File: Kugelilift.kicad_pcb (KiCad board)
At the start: 2 copper layers, 43 x 43.5 mm, 14 parts, among them J1 I2C, J2 TTL, J4 Stepper, SW1 RESET, SW2 MODE, U1 magnetic-charger, U2 TCRT5000, U3 ULN2003A, U4 esp-01f, U5 UA78M33_TO252

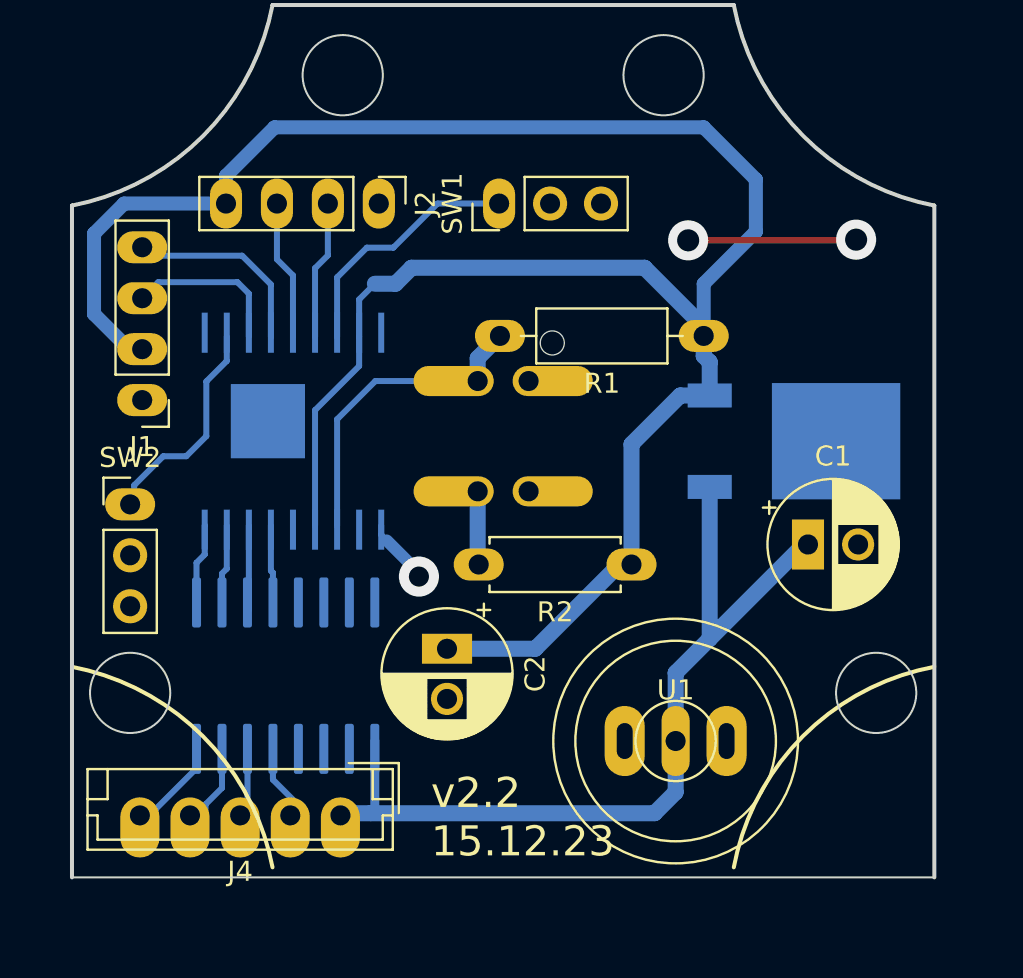
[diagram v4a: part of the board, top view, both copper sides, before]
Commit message: Small adjustments for milling
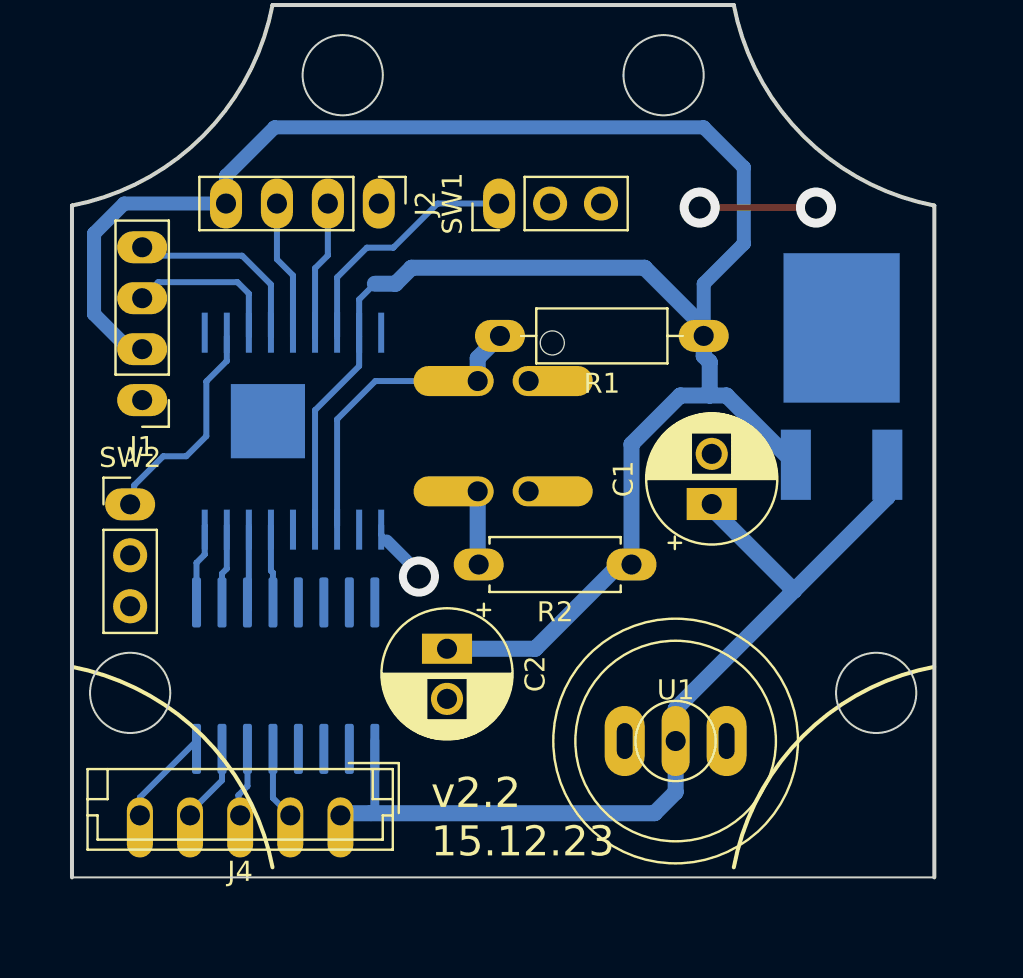
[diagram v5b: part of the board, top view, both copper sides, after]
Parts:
- moved C1 5.21 mm to (132.4, 81.4), turned to 90 degrees
- moved U5 3.85 mm to (138.9, 75.2), turned to 90 degrees
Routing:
- net +3V3: track 109.7 -> 115.0 mm
- net +5V: track 43.8 -> 47.6 mm
- net GND: track 8.59 -> 5.80 mm
